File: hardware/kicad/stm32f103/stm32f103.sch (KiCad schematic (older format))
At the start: 5 parts, among them P1 5VIN, U1 LM1117-3.3

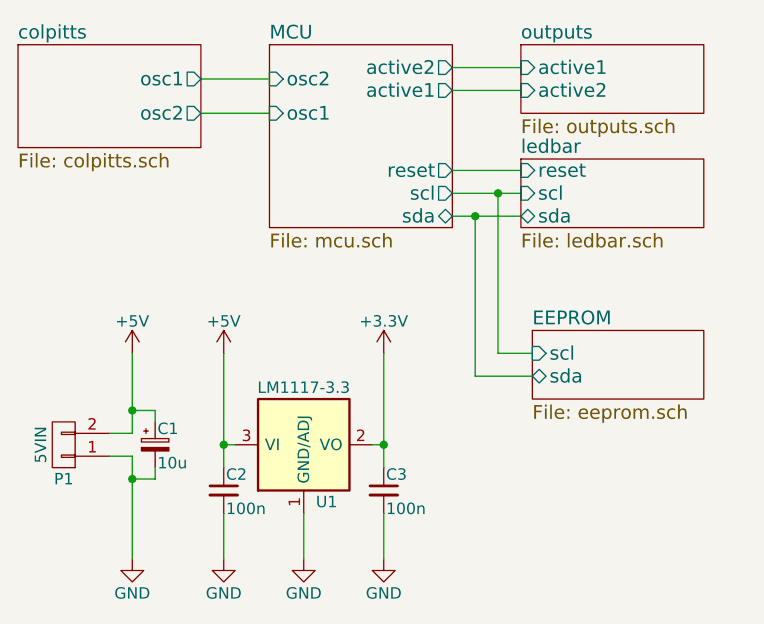
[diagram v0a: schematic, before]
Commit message: hardware/kicad/stm32f103: MCU/LED block ready
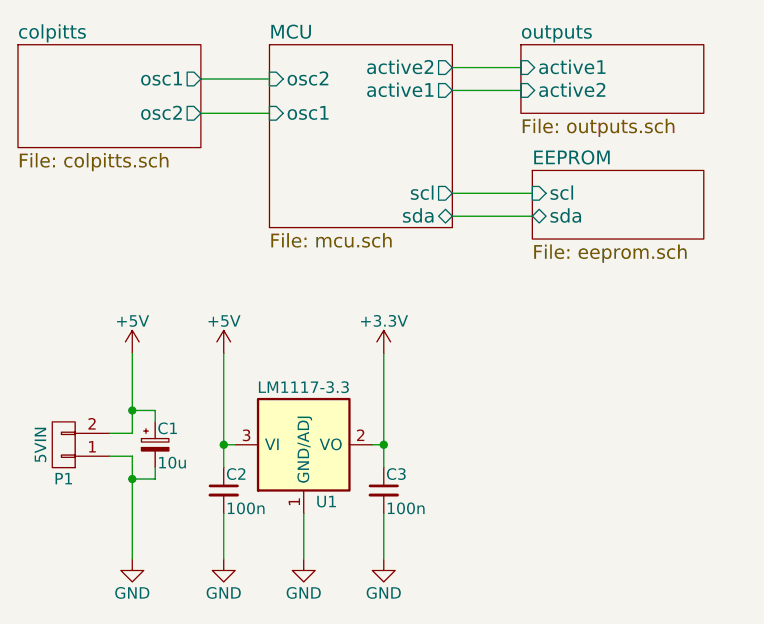
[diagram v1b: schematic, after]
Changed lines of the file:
@@
 LIBS:transformer
 LIBS:stm32
-LIBS:stm32f030-cache
+LIBS:stm32f103-cache
 EELAYER 25 0
 EELAYER END
 $Descr A4 11693 8268
 encoding utf-8
-Sheet 1 6
+Sheet 1 5
 Title ""
 Date ""
@@
 	5100 4650 5000 4650
 Connection ~ 5000 4650
-$Sheet
-S 6700 3250 800  300
-U 58851FF0
-F0 "ledbar" 60
-F1 "ledbar.sch" 60
-F2 "scl" I L 6700 3400 60
-F3 "sda" B L 6700 3500 60
-F4 "reset" I L 6700 3300 60
-$EndSheet
 $Sheet
 S 5600 2750 800  800
@@
 F6 "scl" O R 6400 3400 60
 F7 "sda" B R 6400 3500 60
-F8 "reset" O R 6400 3300 60
-$EndSheet
-Wire Wire Line
-	6400 3300 6700 3300
-Wire Wire Line
-	6400 3400 6700 3400
-Wire Wire Line
-	6400 3500 6700 3500
-$Sheet
-S 6750 4000 750  300
+$EndSheet
+$Sheet
+S 6750 3300 750  300
 U 589C1D7A
 F0 "EEPROM" 60
 F1 "eeprom.sch" 60
-F2 "scl" I L 6750 4100 60
-F3 "sda" B L 6750 4200 60
-$EndSheet
-Wire Wire Line
-	6750 4200 6500 4200
-Wire Wire Line
-	6500 4200 6500 3500
-Connection ~ 6500 3500
-Wire Wire Line
-	6750 4100 6600 4100
-Wire Wire Line
-	6600 4100 6600 3400
-Connection ~ 6600 3400
+F2 "scl" I L 6750 3400 60
+F3 "sda" B L 6750 3500 60
+$EndSheet
+Wire Wire Line
+	6400 3400 6750 3400
+Wire Wire Line
+	6400 3500 6750 3500
 $EndSCHEMATC
